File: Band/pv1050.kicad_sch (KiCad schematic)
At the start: 15 parts

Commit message: finish schematic
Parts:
- added U7: S-1318A33, Package_TO_SOT_SMD:SOT-23-5, symbol S-1318:S-1318A33
- C1, C2, C3, C4: renamed from C?; footprint (none) -> Capacitor_SMD:C_0402_1005Metric
- L1: renamed from L?; footprint (none) -> Inductor_SMD:L_6.3x6.3_H3
- R10, R11, R12, R13, R5, R6, R7, R8, R9: renamed from R?; footprint (none) -> Resistor_SMD:R_0402_1005Metric
- U6: renamed from U?; footprint Package_DFN_QFN:QFN-16-1EP_3x3mm_P0.5mm_EP1.8x1.8mm -> Package_DFN_QFN:VQFN-16-1EP_3x3mm_P0.5mm_EP1.8x1.8mm
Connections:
- net BATT: now also U7.1 (VIN)
- net GND: now also U7.2 (VSS)
- net at U6.11 (VBAT_OK): now also U7.3 (EN)
- new net +3.3V: U7.5 (VOUT)

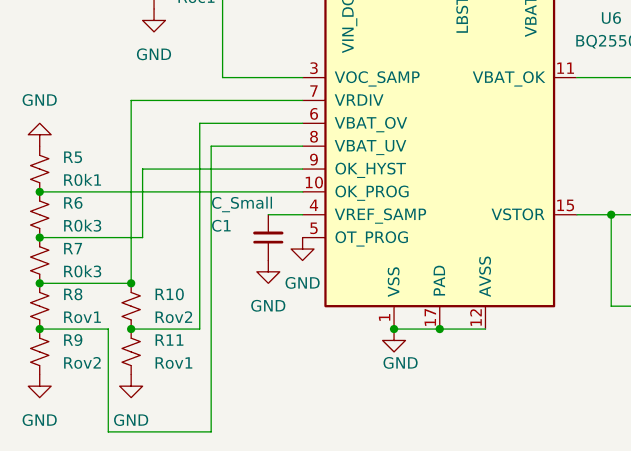
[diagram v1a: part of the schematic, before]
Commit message: preliminary layout
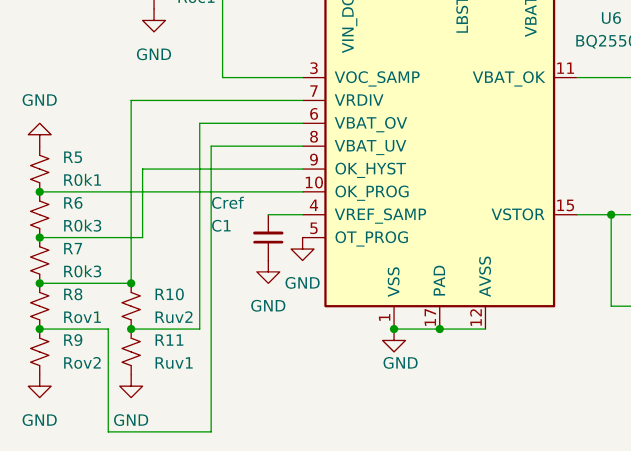
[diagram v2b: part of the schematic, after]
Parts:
- C1: value C_Small -> Cref
- C3: footprint Capacitor_SMD:C_0402_1005Metric -> Capacitor_SMD:C_0805_2012Metric
- L1: footprint Inductor_SMD:L_6.3x6.3_H3 -> Inductor_SMD:L_1806_4516Metric
- R10: value Rov2 -> Ruv2
- R11: value Rov1 -> Ruv1
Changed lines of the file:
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@@
     (property "Reference" "C3" (id 0) (at 160.0263 90.17 90))
     (property "Value" "Cstor" (id 1) (at 160.0263 92.71 90))
-    (property "Footprint" "Capacitor_SMD:C_0402_1005Metric" (id 2) (at 160.02 96.52 0)
+    (property "Footprint" "Capacitor_SMD:C_0805_2012Metric" (id 2) (at 160.02 96.52 0)
       (effects (font (size 1.27 1.27)) hide)
     )
@@
       (effects (font (size 1.27 1.27)) (justify left))
     )
-    (property "Value" "Rov1" (id 1) (at 102.87 113.0299 0)
+    (property "Value" "Ruv1" (id 1) (at 102.87 113.0299 0)
       (effects (font (size 1.27 1.27)) (justify left))
     )
@@
       (effects (font (size 1.27 1.27)) (justify right))
     )
-    (property "Value" "C_Small" (id 1) (at 109.22 95.25 0)
+    (property "Value" "Cref" (id 1) (at 109.22 95.25 0)
       (effects (font (size 1.27 1.27)) (justify right))
     )
@@
       (effects (font (size 1.27 1.27)) (justify left))
     )
-    (property "Value" "Rov2" (id 1) (at 102.87 107.9499 0)
+    (property "Value" "Ruv2" (id 1) (at 102.87 107.9499 0)
       (effects (font (size 1.27 1.27)) (justify left))
     )
@@
       (effects (font (size 1.27 1.27)) (justify left))
     )
-    (property "Footprint" "Inductor_SMD:L_6.3x6.3_H3" (id 2) (at 137.16 62.23 0)
-      (effects (font (size 1.27 1.27)) hide)
-    )
+    (property "Footprint" "Inductor_SMD:L_1806_4516Metric" (id 2) (at 137.16 62.23 0)
+      (effects (font (size 1.27 1.27)) hide)
+    )

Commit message: v1 final changes
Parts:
- L1: footprint Inductor_SMD:L_1806_4516Metric -> Inductor_SMD:L_1210_3225Metric
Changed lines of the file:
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@@
       (effects (font (size 1.27 1.27)) (justify left))
     )
-    (property "Footprint" "Inductor_SMD:L_1806_4516Metric" (id 2) (at 137.16 62.23 0)
+    (property "Footprint" "Inductor_SMD:L_1210_3225Metric" (id 2) (at 137.16 62.23 0)
       (effects (font (size 1.27 1.27)) hide)
     )
